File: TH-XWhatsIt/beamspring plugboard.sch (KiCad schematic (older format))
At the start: 4 parts, among them J6 BEAMSPRING PLUGBOARD COLUMNS, J7 BEAMSPRING PLUGBOARD CONNECTOR, J8 BEAMSPRING PLUGBOARD ROWS

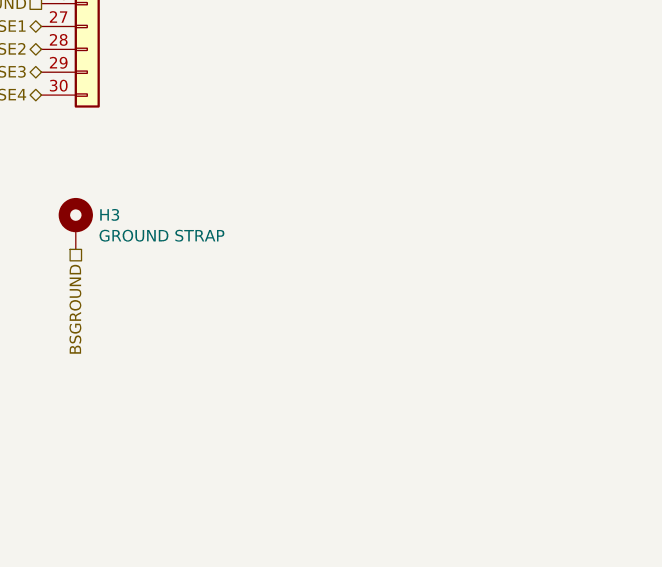
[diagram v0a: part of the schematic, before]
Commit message: Added big oval mounting hole, Y position not yet final
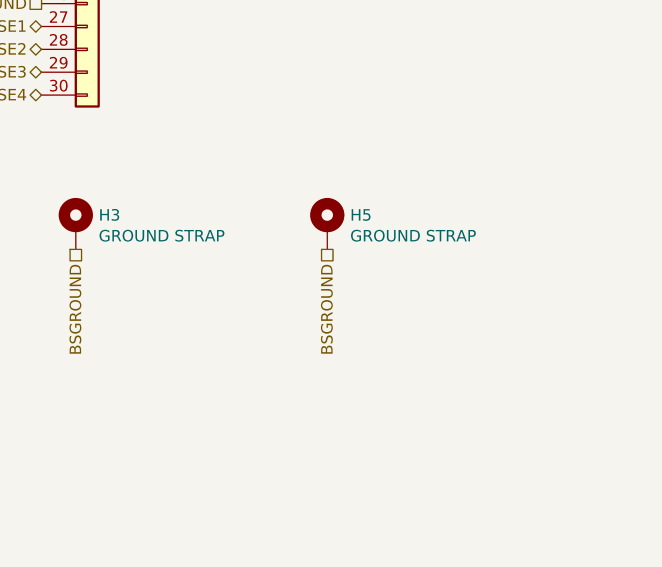
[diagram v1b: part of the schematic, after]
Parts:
- added H5: GROUND STRAP, TH-XWhatsIt:BeamSpringGroundingMountingHole, symbol Mechanical:MountingHole_Pad
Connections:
- net BSGROUND: now also H5.1
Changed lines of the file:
@@
 Text HLabel 5150 4775 3    50   UnSpc ~ 0
 BSGROUND
+$Comp
+L Mechanical:MountingHole_Pad H5
+U 1 1 5F892130
+P 6250 4675
+F 0 "H5" H 6350 4724 50  0000 L CNN
+F 1 "GROUND STRAP" H 6350 4633 50  0000 L CNN
+F 2 "TH-XWhatsIt:BeamSpringGroundingMountingHole" H 6250 4675 50  0001 C CNN
+F 3 "~" H 6250 4675 50  0001 C CNN
+	1    6250 4675
+	1    0    0    -1
+$EndComp
+Text HLabel 6250 4775 3    50   UnSpc ~ 0
+BSGROUND
 $EndSCHEMATC
